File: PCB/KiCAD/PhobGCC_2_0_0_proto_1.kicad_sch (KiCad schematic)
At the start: 110 parts, among them J1 Conn_01x06_Female, J11 Conn_01x02, J14 Conn_01x06, J15 Conn_01x06, J2 Conn_01x02, J3 Conn_01x02, J4 Conn_01x01, J5 Rumble, J6 Conn_01x06, J8 USB_B_Micro, Q1 Q_NMOS_GSD, Q2 Q_PMOS_GDS, Q3 Q_NMOS_GSD, SW1 A, SW10 Dup, SW11 Dright, SW12 Ddown, SW2 B, SW3 X, SW4 Y, SW5 Start, SW6 L, SW7 R, SW8 Z, SW9 Dleft, U1 MCP3202, U10 DRV5055A3xDBZxQ1, U11 DRV5055A3xDBZxQ1, U12 USBLC6-2P6, U13 USBLC6-2P6, U2 Stickbox_Assembly_Main, U3 MCP3202, U4 DRV5055A3xDBZxQ1, U5 Stickbox_Assembly_CStick, U6 AMS1117-3.3, U7 W25Q128JVS, U8 RP2040, U9 DRV5055A3xDBZxQ1, Y1 Crystal_GND24

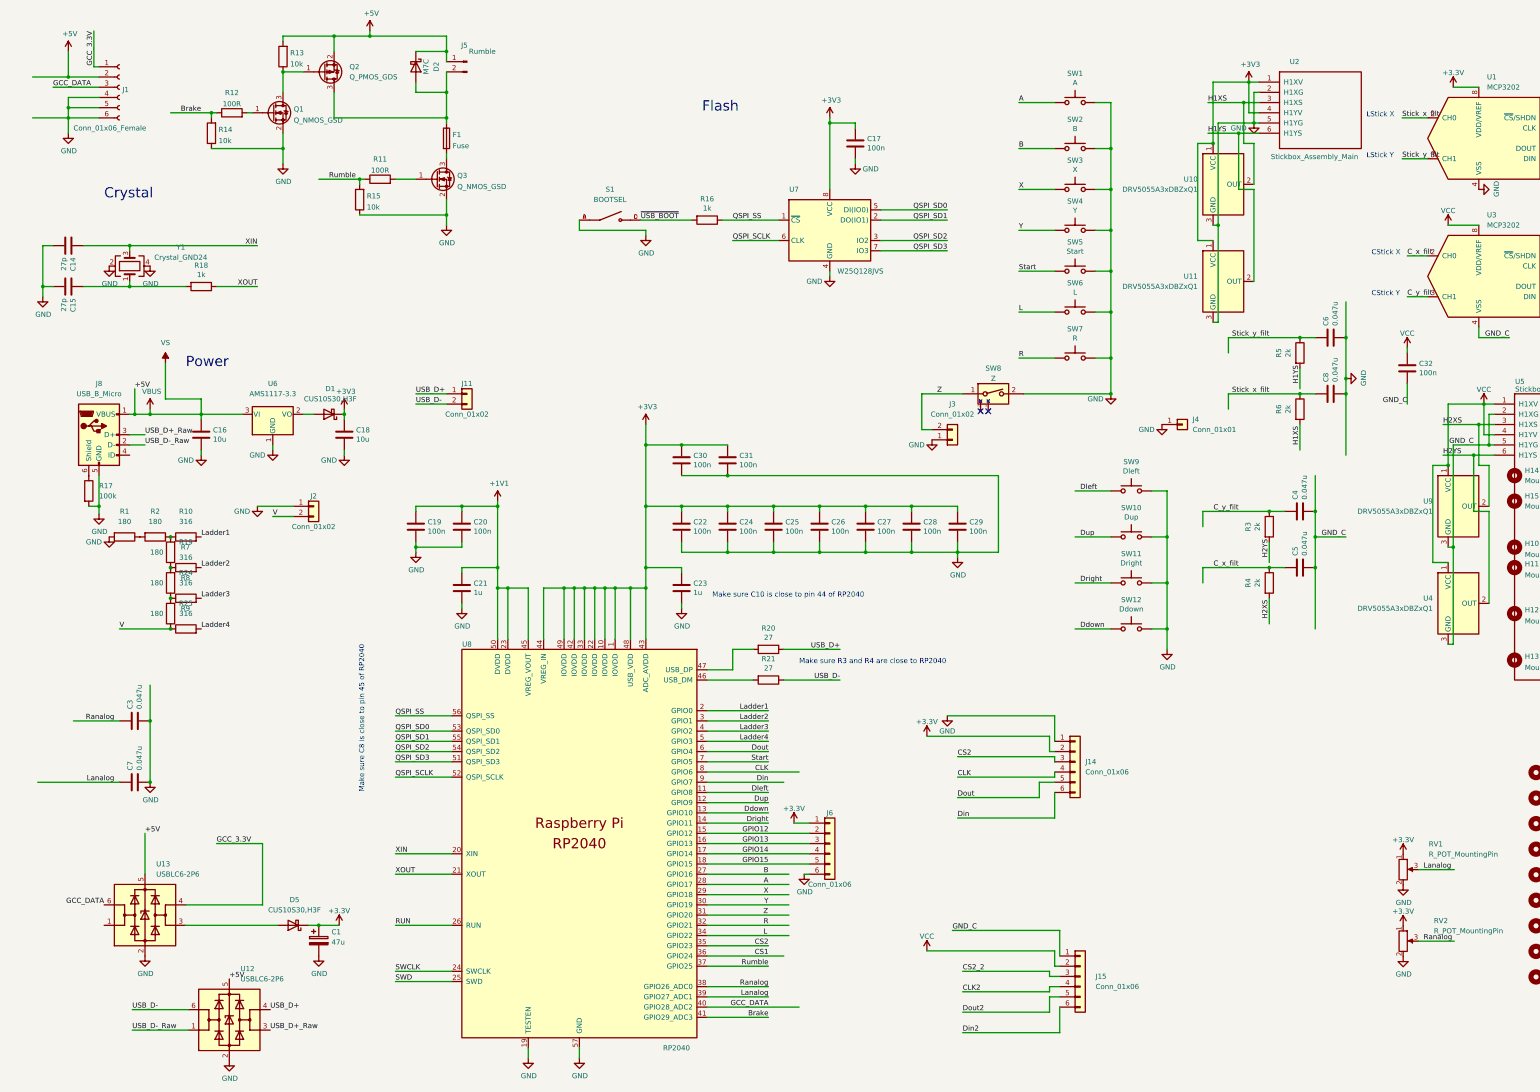
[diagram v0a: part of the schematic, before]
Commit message: NaxGCC Changes:
- update to KiCad 8
- replace micro USB & GCC connector with USB C
- add some JLCPCB symbols, footprints & models
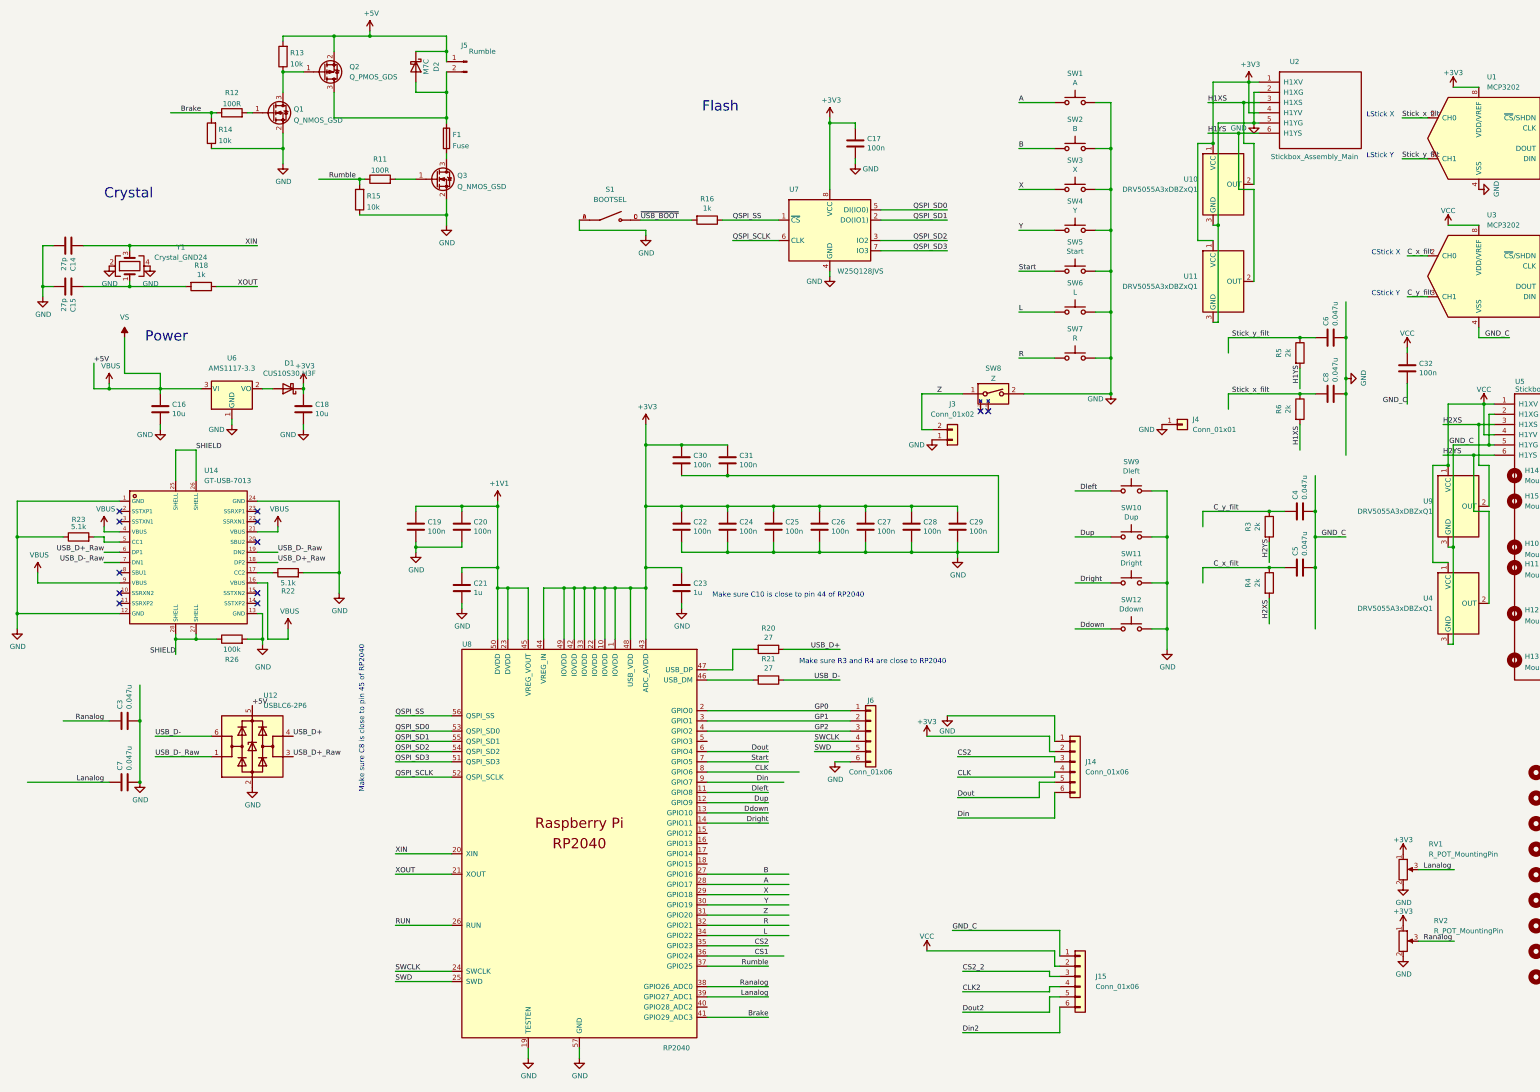
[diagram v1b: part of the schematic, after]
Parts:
- removed C1: 47u, Capacitor_Tantalum_SMD:CP_EIA-3528-12_Kemet-T_Pad1.50x2.35mm_HandSolder, symbol Device:C_Polarized
- removed D5: CUS10S30,H3F, Diode_SMD:D_SOD-323, symbol Diode:MBR0520
- removed J1: Conn_01x06_Female, PhobGCC_2_0_0_footprints:GCC_Header_Straight_1x06_Pitch2.00mm, symbol Connector:Conn_01x06_Female
- removed J11, J2: Conn_01x02, PhobGCC_2_0_0_footprints:PinHeader_1x02_P2.00mm_Vertical, symbol Connector_Generic:Conn_01x02
- removed J8: USB_B_Micro, PhobGCC_2_0_0_footprints:USB_Micro-B_Amphenol_10118194_Horizontal, symbol Connector:USB_B_Micro
- removed R1, R2, R7, R8, R9: 180, PhobGCC_2_0_0_footprints:R_0402_1005Metric, symbol Device:R
- removed R10, R19, R24, R25: 316, PhobGCC_2_0_0_footprints:R_0402_1005Metric, symbol Device:R
- removed R17: 100k, Resistor_SMD:R_0603_1608Metric_Pad0.98x0.95mm_HandSolder, symbol Device:R
- removed U13: USBLC6-2P6, Package_TO_SOT_SMD:SOT-666, symbol Power_Protection:USBLC6-2P6
- added R22, R23: 5.1k, Resistor_SMD:R_0402_1005Metric, symbol Device:R
- added R26: 100k, Resistor_SMD:R_0603_1608Metric_Pad0.98x0.95mm_HandSolder, symbol Device:R
- added U14: GT-USB-7013, footprint:USB-C-SMD_GT-USB-7013, symbol GT-USB-7013:GT-USB-7013
- S1: LCSC (none) -> C318884
- Y1: LCSC C40395 -> C403945
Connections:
- net +3V3: no longer J6.1 (Pin_1)
- net +5V: now also U14.16 (VBUS), U14.21 (VBUS), U14.4 (VBUS), U14.9 (VBUS)
- net GND: now also R22.2, R23.1, R26.2, U14.1 (GND), U14.12 (GND), U14.13 (GND), U14.24 (GND)
- net SWCLK: now also J6.4 (Pin_4)
- net SWD: now also J6.5 (Pin_5)
- net USB_D+_Raw: now also U14.18 (DP2), U14.6 (DP1)
- net USB_D-_Raw: now also U14.19 (DN2), U14.7 (DN1)
- net GCC_DATA: no longer names the net of U8.40 (GPIO28_ADC2)
- net GPIO12: no longer names the net of U8.15 (GPIO12)
- net GPIO12: no longer J6.2 (Pin_2)
- net GPIO13: no longer names the net of U8.16 (GPIO13)
- net GPIO13: no longer J6.3 (Pin_3)
- net GPIO14: no longer names the net of U8.17 (GPIO14)
- net GPIO14: no longer J6.4 (Pin_4)
- net GPIO15: no longer names the net of U8.18 (GPIO15)
- net GPIO15: no longer J6.5 (Pin_5)
- net Ladder1 renamed GP0
- net GP0: now also J6.1 (Pin_1)
- net Ladder2 renamed GP1
- net GP1: now also J6.2 (Pin_2)
- net Ladder3 renamed GP2
- net GP2: now also J6.3 (Pin_3)
- net Ladder4: no longer names the net of U8.5 (GPIO3)
- new net: R22.1, U14.17 (CC2)
- new net: R23.2, U14.5 (CC1)
- new net SHIELD: R26.1, U14.25 (SHELL), U14.26 (SHELL), U14.27 (SHELL), U14.28 (SHELL)
- no-connect marks 2 -> 12
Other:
- moved on the sheet: C16, C18, C3, C7, D1, J6, U12, U6
